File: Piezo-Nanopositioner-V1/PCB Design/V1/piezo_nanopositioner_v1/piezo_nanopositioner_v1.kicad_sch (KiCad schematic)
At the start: 34 parts, among them J1 Conn_01x10_Pin, J2 RF2-04A-T-00-50-G, J3 Conn_01x03_Socket, U1 TDA2050, U2 DAC0800LCM, U4 TL431AIDBZR

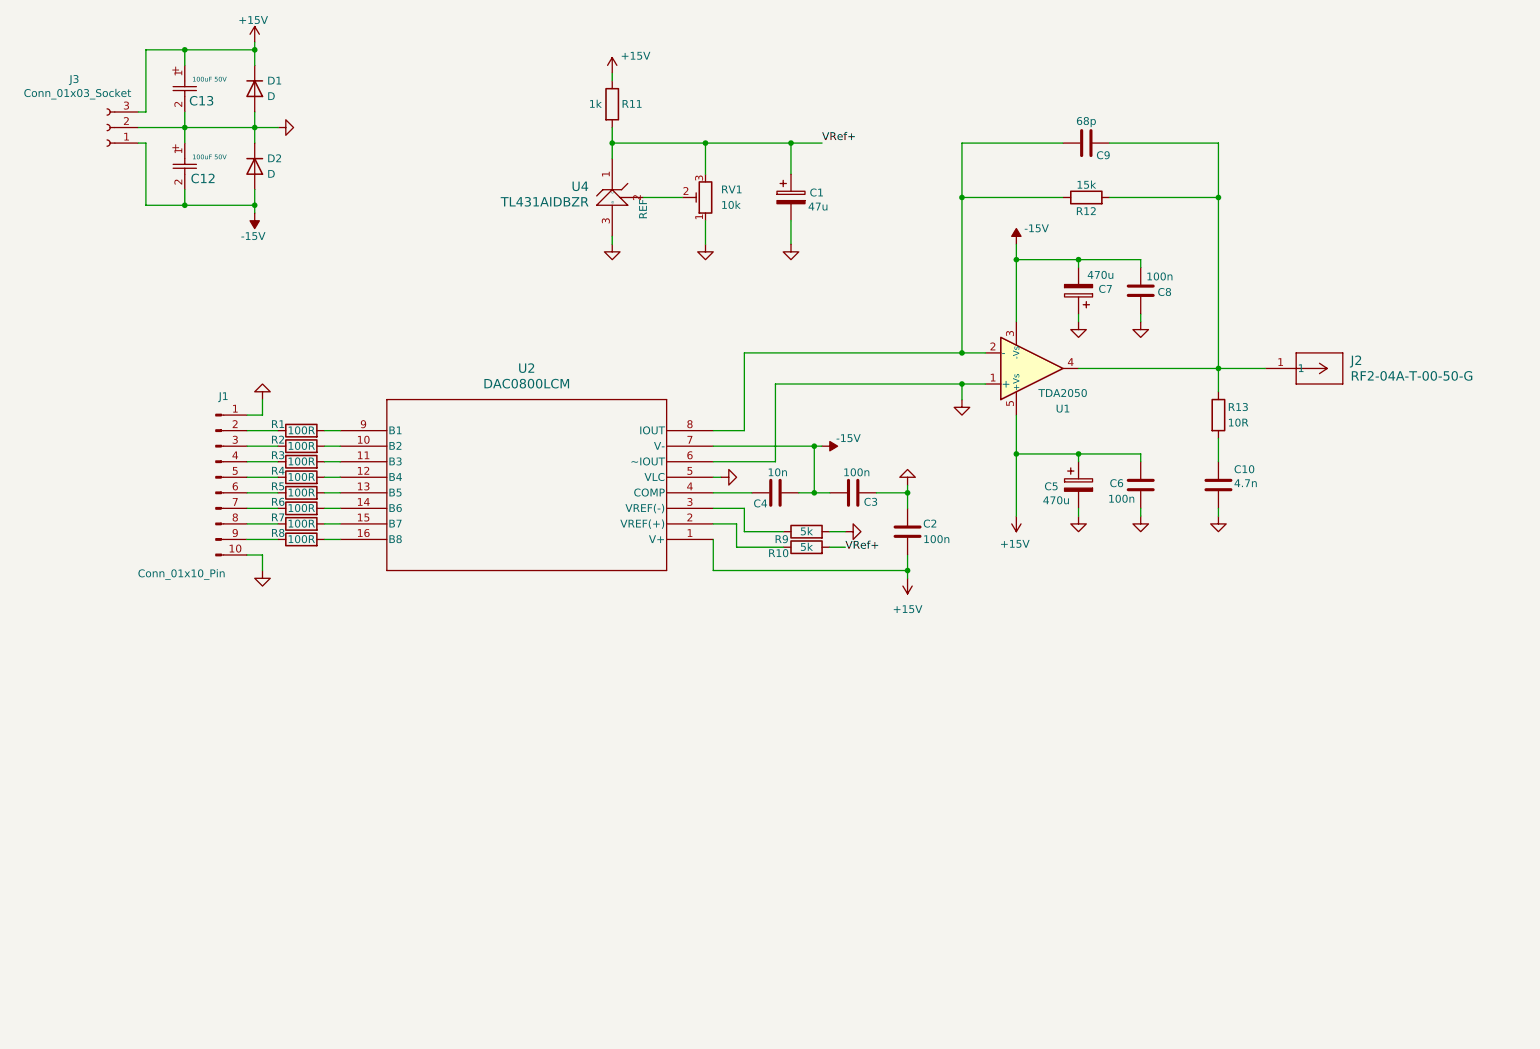
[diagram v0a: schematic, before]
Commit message: finalized schematic, added hierarchical sheets for X,Y,Z circuit. Added all part fingerprints.
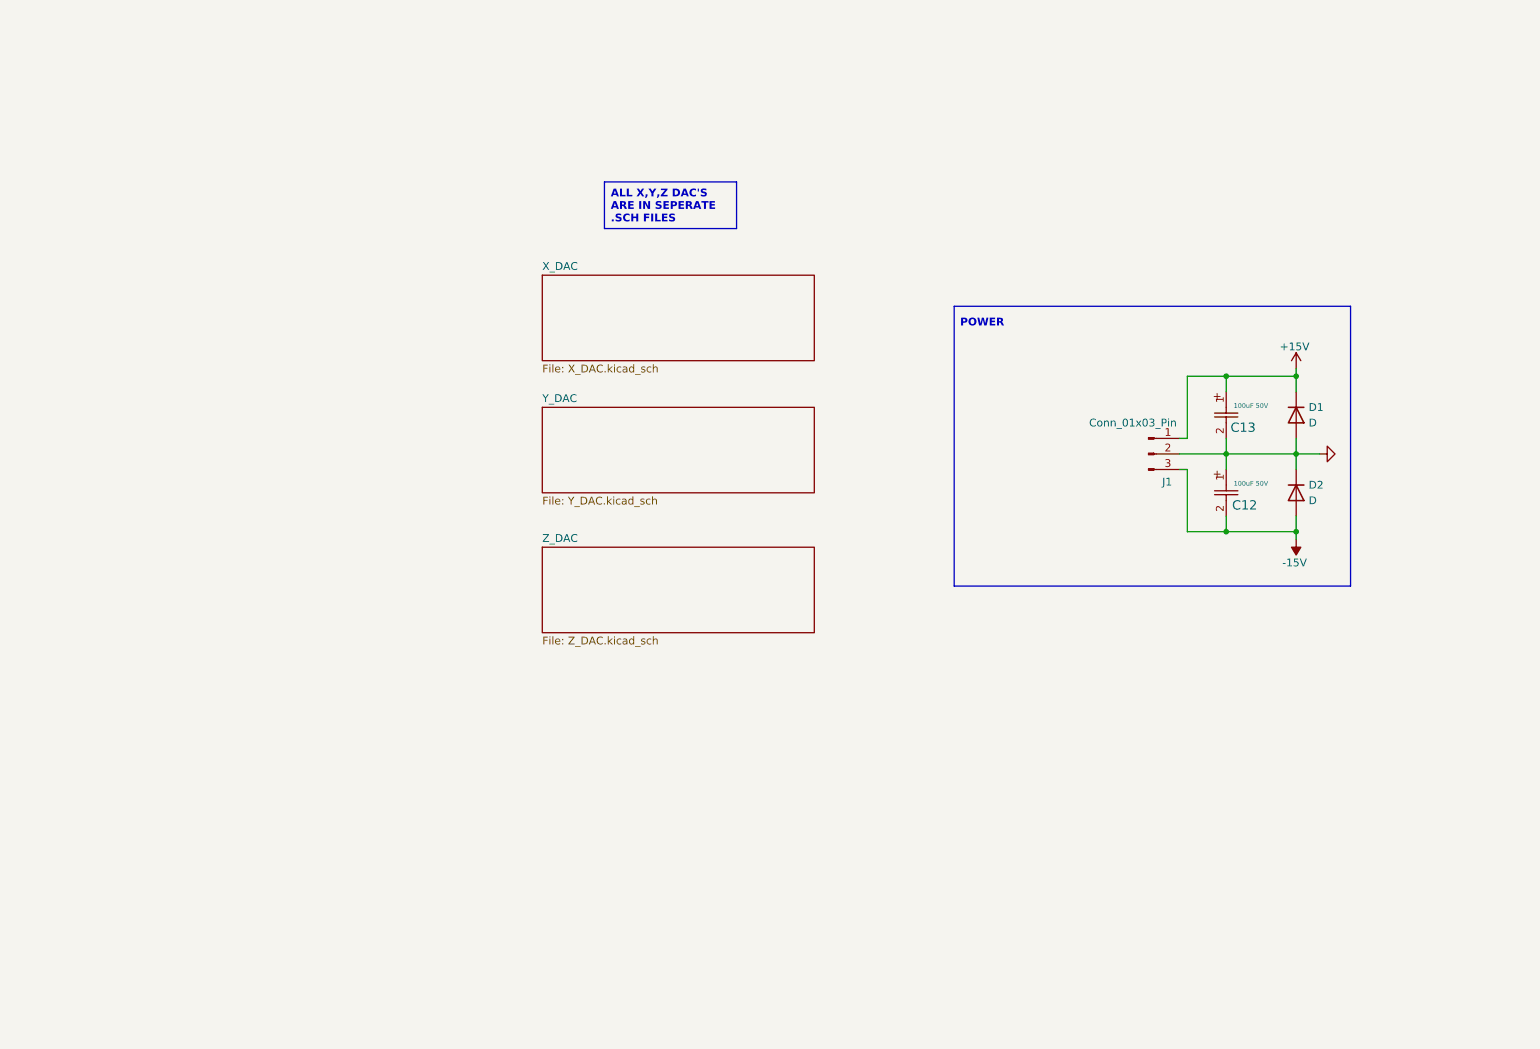
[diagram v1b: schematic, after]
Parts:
- removed C1: 47u, symbol Device:C_Polarized
- removed C10: 4.7n, symbol Device:C
- removed C2, C3, C6, C8: 100n, symbol Device:C
- removed C4: 10n, symbol Device:C
- removed C5, C7: 470u, symbol Device:C_Polarized
- removed C9: 68p, symbol Device:C
- removed J1: Conn_01x10_Pin, symbol Connector:Conn_01x10_Pin
- removed J2: RF2-04A-T-00-50-G, RF:CONN_RF2-04A-T-00-50-G_ADM, symbol SMA_Connector:RF2-04A-T-00-50-G
- removed J3: Conn_01x03_Socket, symbol Connector:Conn_01x03_Socket
- removed R1, R2, R3, R4, R5, R6, R7, R8: 100R, symbol Device:R
- removed R10, R9: 5k, symbol Device:R
- removed R11: 1k, symbol Device:R
- removed R12: 15k, symbol Device:R
- removed R13: 10R, symbol Device:R
- removed RV1: 10k, symbol Device:R_Potentiometer_Trim
- removed U1: TDA2050, Package_TO_SOT_THT:TO-220-5_P3.4x3.7mm_StaggerOdd_Lead3.8mm_Vertical, symbol Amplifier_Audio:TDA2050
- removed U2: DAC0800LCM, M16A_TEX, symbol DAC0800LCM_SMT:DAC0800LCM
- removed U4: TL431AIDBZR, DBZ0003A_N, symbol TL431AIDBZR:TL431AIDBZR
- added J1: Conn_01x03_Pin, Connector_PinHeader_2.54mm:PinHeader_1x03_P2.54mm_Vertical, symbol Connector:Conn_01x03_Pin
- D1, D2: footprint (none) -> Diode_THT:DO-41_DIO
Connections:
- net +15V: now also J1.1 (Pin_1)
- net -15V: now also J1.3 (Pin_3)
- net GND: now also J1.2 (Pin_2)
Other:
- added sheet X_DAC (X_DAC.kicad_sch)
- added sheet Y_DAC (Y_DAC.kicad_sch)
- added sheet Z_DAC (Z_DAC.kicad_sch)
- note added: "POWER"
- moved on the sheet: C12, C13, D1, D2

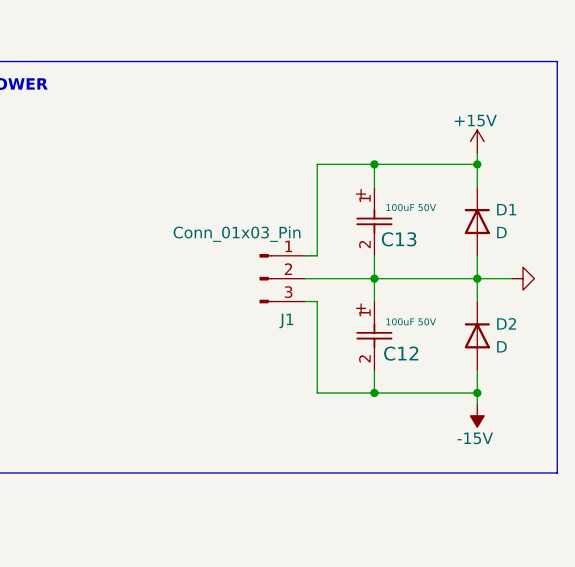
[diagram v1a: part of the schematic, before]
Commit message: Created rough PCB component layout for Z actuator.
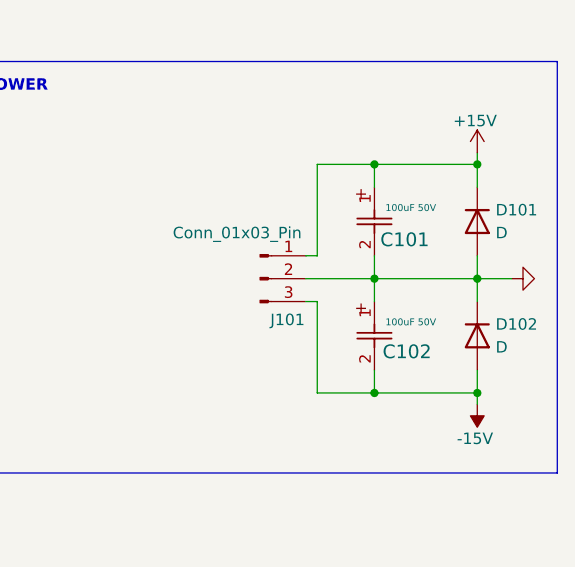
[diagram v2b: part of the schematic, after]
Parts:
- renumbered C13 to C101, C12 to C102, D1 to D101, D2 to D102, J1 to J101
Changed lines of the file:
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@@
 		(on_board yes)
 		(dnp no)
-		(property "Reference" "#PWR021"
+		(property "Reference" "#PWR0102"
 			(at 229.87 99.06 0)
 			(effects
@@
 			(project ""
 				(path "/7b2a32d8-cc7d-471d-a8eb-eea62713ed45"
-					(reference "#PWR021")
+					(reference "#PWR0102")
 					(unit 1)
 				)
@@
 		(on_board yes)
 		(dnp no)
-		(property "Reference" "C13"
-			(at 223.266 84.582 90)
+		(property "Reference" "C101"
+			(at 224.536 84.582 90)
 			(effects
 				(font
@@
 			(project "piezo_nanopositioner_v1"
 				(path "/7b2a32d8-cc7d-471d-a8eb-eea62713ed45"
-					(reference "C13")
+					(reference "C101")
 					(unit 1)
 				)
@@
 		(on_board yes)
 		(dnp no)
-		(property "Reference" "J1"
+		(property "Reference" "J101"
 			(at 208.788 93.472 0)
 			(effects
@@
 			(project ""
 				(path "/7b2a32d8-cc7d-471d-a8eb-eea62713ed45"
-					(reference "J1")
+					(reference "J101")
 					(unit 1)
 				)
@@
 		(on_board yes)
 		(dnp no)
-		(property "Reference" "#PWR020"
+		(property "Reference" "#PWR0101"
 			(at 229.87 78.74 0)
 			(effects
@@
 			(project ""
 				(path "/7b2a32d8-cc7d-471d-a8eb-eea62713ed45"
-					(reference "#PWR020")
+					(reference "#PWR0101")
 					(unit 1)
 				)
@@
 		(dnp no)
 		(fields_autoplaced yes)
-		(property "Reference" "#PWR022"
+		(property "Reference" "#PWR0103"
 			(at 240.03 88.9 0)
 			(effects
@@
 			(project ""
 				(path "/7b2a32d8-cc7d-471d-a8eb-eea62713ed45"
-					(reference "#PWR022")
+					(reference "#PWR0103")
 					(unit 1)
 				)
@@
 		(on_board yes)
 		(dnp no)
-		(property "Reference" "C12"
-			(at 223.52 97.282 90)
+		(property "Reference" "C102"
+			(at 224.79 97.028 90)
 			(effects
 				(font
@@
 			(project ""
 				(path "/7b2a32d8-cc7d-471d-a8eb-eea62713ed45"
-					(reference "C12")
+					(reference "C102")
 					(unit 1)
 				)
@@
 		(on_board yes)
 		(dnp no)
-		(property "Reference" "D1"
+		(property "Reference" "D101"
 			(at 231.902 81.28 90)
 			(effects
@@
 			(project ""
 				(path "/7b2a32d8-cc7d-471d-a8eb-eea62713ed45"
-					(reference "D1")
+					(reference "D101")
 					(unit 1)
 				)
@@
 		(on_board yes)
 		(dnp no)
-		(property "Reference" "D2"
+		(property "Reference" "D102"
 			(at 231.902 93.98 90)
 			(effects
@@
 			(project "piezo_nanopositioner_v1"
 				(path "/7b2a32d8-cc7d-471d-a8eb-eea62713ed45"
-					(reference "D2")
-					(unit 1)
-				)
+					(reference "D102")
+					(unit 1)
+				)

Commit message: added heatsink to XYZ schematics, finalized BOM, minimal PCB layout done.
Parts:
- C101, C102: Distributor Link (none) -> https://www.digikey.ca/en/products/detail/rubycon/50YXJ100M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; Manufacturer (none) -> Rubycon; Manufacturer Part (none) -> 50YXJ100MT78X11.5
- D101, D102: Distributor Link (none) -> https://www.digikey.ca/en/products/detail/onsemi/1N4001RLG/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; Manufacturer (none) -> onsemi; Manufacturer Part (none) -> 1N4001RLG
- J101: Distributor Link (none) -> https://www.digikey.ca/en/products/detail/w%C3%BCrth-elektr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; Manufacturer (none) -> Würth Elektronik; Manufacturer Part (none) -> 61300311121
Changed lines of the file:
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@@
+			)
+		)
+		(property "Distributor Link" "https://www.digikey.ca/en/products/detail/rubycon/50YXJ100MT78X11-5/3134938"
+			(at 218.44 78.74 0)
+			(effects
+				(font
+					(size 1.27 1.27)
+				)
+				(hide yes)
+			)
+		)
+		(property "Manufacturer" "Rubycon"
+			(at 218.44 78.74 0)
+			(effects
+				(font
+					(size 1.27 1.27)
+				)
+				(hide yes)
+			)
+		)
+		(property "Manufacturer Part" "50YXJ100MT78X11.5"
+			(at 218.44 78.74 0)
+			(effects
+				(font
+					(size 1.27 1.27)
+				)
+				(hide yes)
 			)
 		)
@@
 		)
 		(property "Description" "Generic connector, single row, 01x03, script generated"
+			(at 205.74 88.9 0)
+			(effects
+				(font
+					(size 1.27 1.27)
+				)
+				(hide yes)
+			)
+		)
+		(property "Distributor Link" "https://www.digikey.ca/en/products/detail/w%C3%BCrth-elektronik/61300311121/4846825 "
+			(at 205.74 88.9 0)
+			(effects
+				(font
+					(size 1.27 1.27)
+				)
+				(hide yes)
+			)
+		)
+		(property "Manufacturer" "Würth Elektronik "
+			(at 205.74 88.9 0)
+			(effects
+				(font
+					(size 1.27 1.27)
+				)
+				(hide yes)
+			)
+		)
+		(property "Manufacturer Part" "61300311121 "
 			(at 205.74 88.9 0)
 			(effects
@@
 			)
 		)
+		(property "Distributor Link" "https://www.digikey.ca/en/products/detail/rubycon/50YXJ100MT78X11-5/3134938"
+			(at 218.44 91.44 0)
+			(effects
+				(font
+					(size 1.27 1.27)
+				)
+				(hide yes)
+			)
+		)
+		(property "Manufacturer" "Rubycon"
+			(at 218.44 91.44 0)
+			(effects
+				(font
+					(size 1.27 1.27)
+				)
+				(hide yes)
+			)
+		)
+		(property "Manufacturer Part" "50YXJ100MT78X11.5"
+			(at 218.44 91.44 0)
+			(effects
+				(font
+					(size 1.27 1.27)
+				)
+				(hide yes)
+			)
+		)
 		(pin "1"
 		)
@@
 			)
 		)
+		(property "Distributor Link" "https://www.digikey.ca/en/products/detail/onsemi/1N4001RLG/917621 "
+			(at 229.87 82.55 0)
+			(effects
+				(font
+					(size 1.27 1.27)
+				)
+				(hide yes)
+			)
+		)
+		(property "Manufacturer" "onsemi "
+			(at 229.87 82.55 0)
+			(effects
+				(font
+					(size 1.27 1.27)
+				)
+				(hide yes)
+			)
+		)
+		(property "Manufacturer Part" "1N4001RLG "
+			(at 229.87 82.55 0)
+			(effects
+				(font
+					(size 1.27 1.27)
+				)
+				(hide yes)
+			)
+		)
 		(pin "2"
 		)
@@
 			(at 229.87 95.25 0)
 			(effects
+				(font
+					(size 1.27 1.27)
+				)
+				(hide yes)
+			)
+		)
+		(property "Distributor Link" "https://www.digikey.ca/en/products/detail/onsemi/1N4001RLG/917621 "
+			(at 229.87 95.25 0)
+			(effects
+				(font
+					(size 1.27 1.27)
+				)
+				(hide yes)
+			)
+		)
+		(property "Manufacturer" "onsemi "
+			(at 229.87 95.25 0)
+			(effects
+				(font
+					(size 1.27 1.27)
+				)
+				(hide yes)
+			)
+		)
+		(property "Manufacturer Part" "1N4001RLG "
+			(at 229.87 95.25 0)
+			(effects

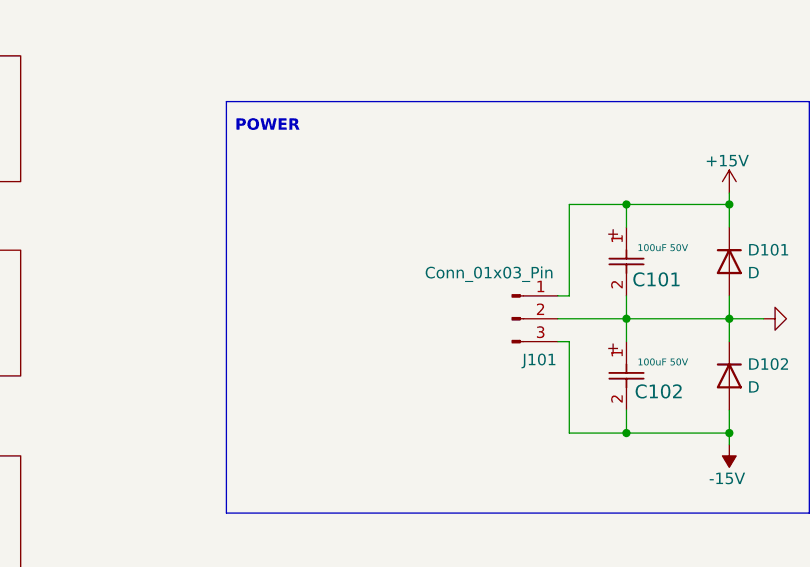
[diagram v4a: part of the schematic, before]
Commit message: Added 3d model files for component. Finished connecting the fill zones. Added mounting holes. Added pictures of pcb and layout.
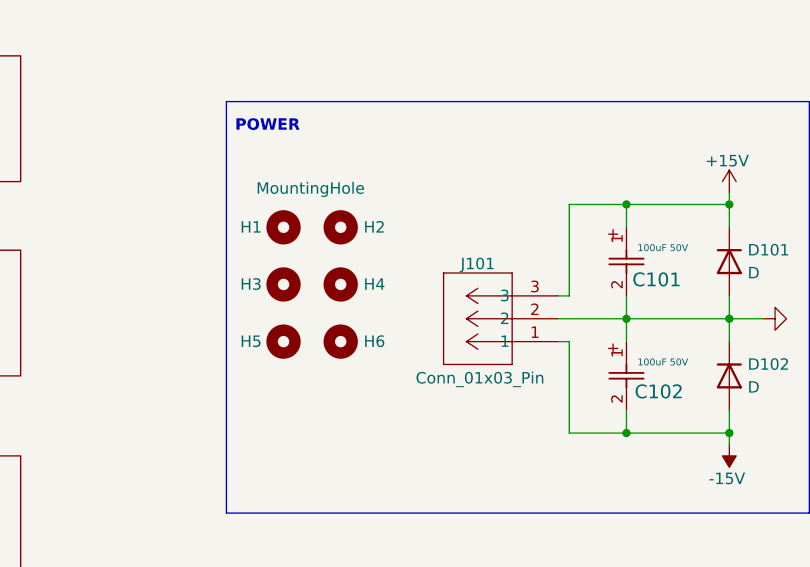
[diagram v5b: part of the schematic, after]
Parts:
- added H1, H2, H3, H4, H5, H6: MountingHole, MountingHole:MountingHole_3.2mm_M3_Pad_Via, symbol Mechanical:MountingHole
- J101: footprint Connector_PinHeader_2.54mm:PinHeader_1x03_P2.54mm_Vertical -> CONN_39880-0303_MOL; symbol Connector:Conn_01x03_Pin -> Molex Connector:398800303
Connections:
- net +15V: now also J101.3; no longer J101.1 (Pin_1)
- net -15V: now also J101.1; no longer J101.3 (Pin_3)
